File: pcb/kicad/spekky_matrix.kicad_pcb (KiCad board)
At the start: 2 copper layers, 153 x 95.8 mm, 330 parts, among them J1 USB_B_Micro, J2 Conn_ARM_JTAG_SWD_10, Q1 DMP3125L-7, Q2 DMP3125L-7, Q3 DMP3125L-7, Q4 DMP3125L-7, Q5 DMP3125L-7, Q6 DMP3125L-7, Q7 DMP3125L-7, Q8 DMP3125L-7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

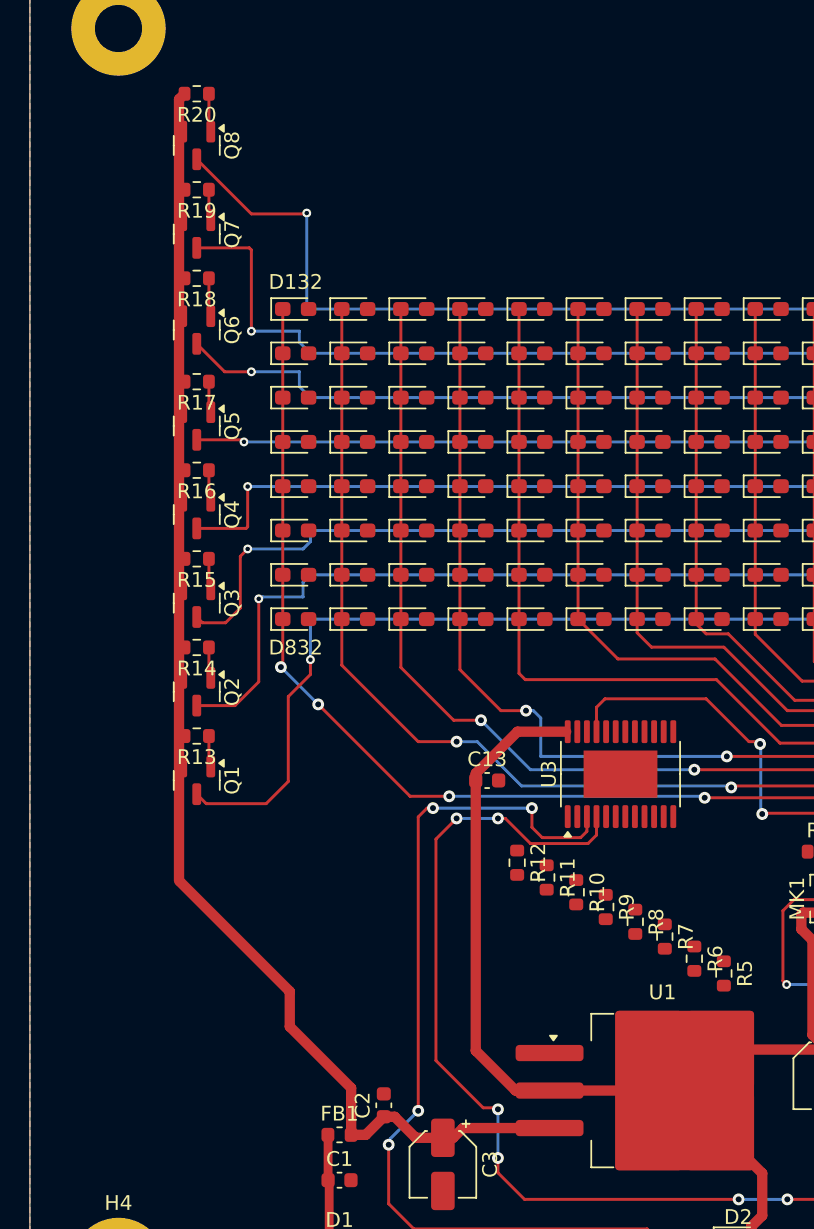
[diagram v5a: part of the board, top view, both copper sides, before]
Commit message: Connect mosfet resistor network traces
- With a GND via across signal vias
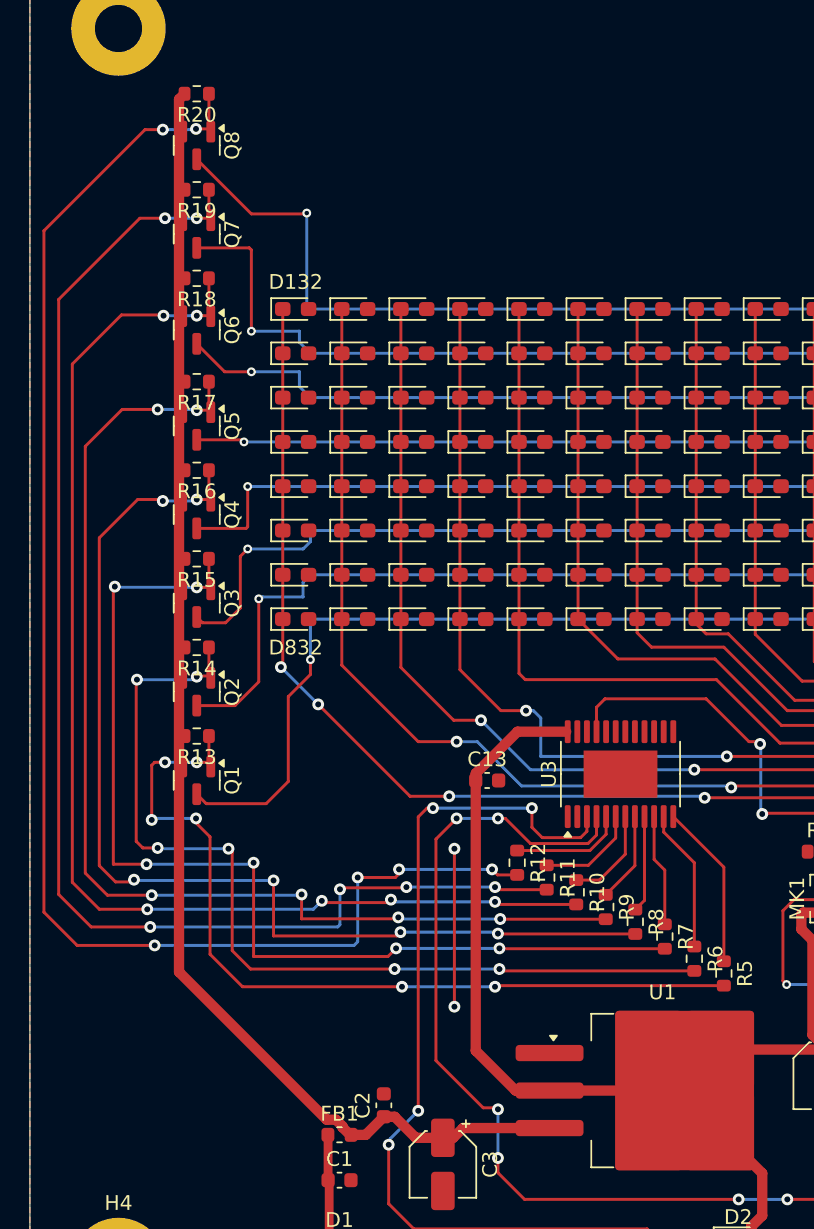
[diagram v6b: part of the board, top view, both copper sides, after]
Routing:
- net Net-(Q8-G): track 2.61 -> 101.0 mm, vias 0 -> 6
- net Net-(Q7-G): track 2.11 -> 91.6 mm, vias 0 -> 6
- net Net-(Q6-G): track 2.61 -> 83.9 mm, vias 0 -> 6
- net Net-(Q5-G): track 2.11 -> 78.5 mm, vias 0 -> 6
- net Net-(Q4-G): track 2.11 -> 73.8 mm, vias 0 -> 6
- net Net-(Q3-G): track 2.11 -> 71.3 mm, vias 0 -> 6
- net Net-(Q2-G): track 2.11 -> 63.6 mm, vias 0 -> 6
- net Net-(Q1-G): track 2.11 -> 58.4 mm, vias 0 -> 6
- net /LED DRIVING/~{OUT7}: track 0.00 -> 11.2 mm
- net GND: track 5.18 -> 15.8 mm, vias 0 -> 2
- net /LED DRIVING/~{OUT6}: track 0.00 -> 9.66 mm
- net /LED DRIVING/~{OUT0}: track 0.00 -> 7.68 mm
- net /LED DRIVING/~{OUT5}: track 0.00 -> 7.60 mm
- net /LED DRIVING/~{OUT1}: track 0.00 -> 6.89 mm
- net /LED DRIVING/~{OUT2}: track 0.00 -> 6.60 mm
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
